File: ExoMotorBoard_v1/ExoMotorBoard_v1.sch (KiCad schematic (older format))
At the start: 3 parts, among them IC1 DSPIC33FJ128MC802-I_SP, U1 MIC5219-3.3YMM

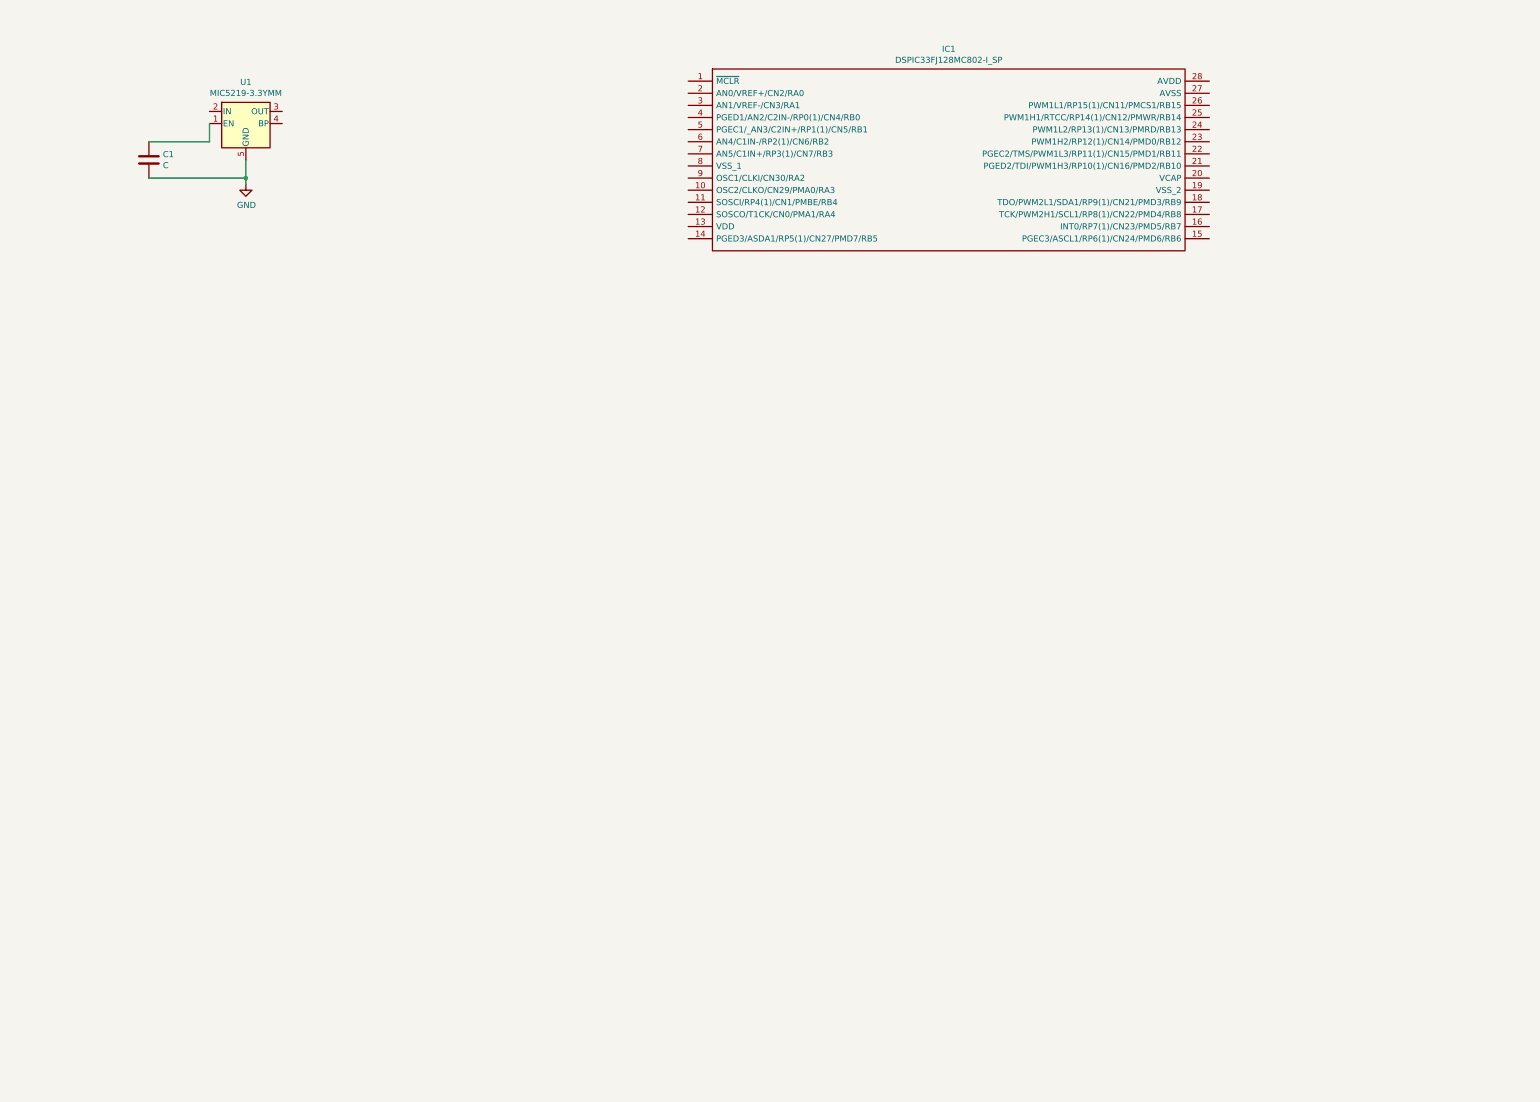
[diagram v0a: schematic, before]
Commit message: 3.3v regulator circuit updated
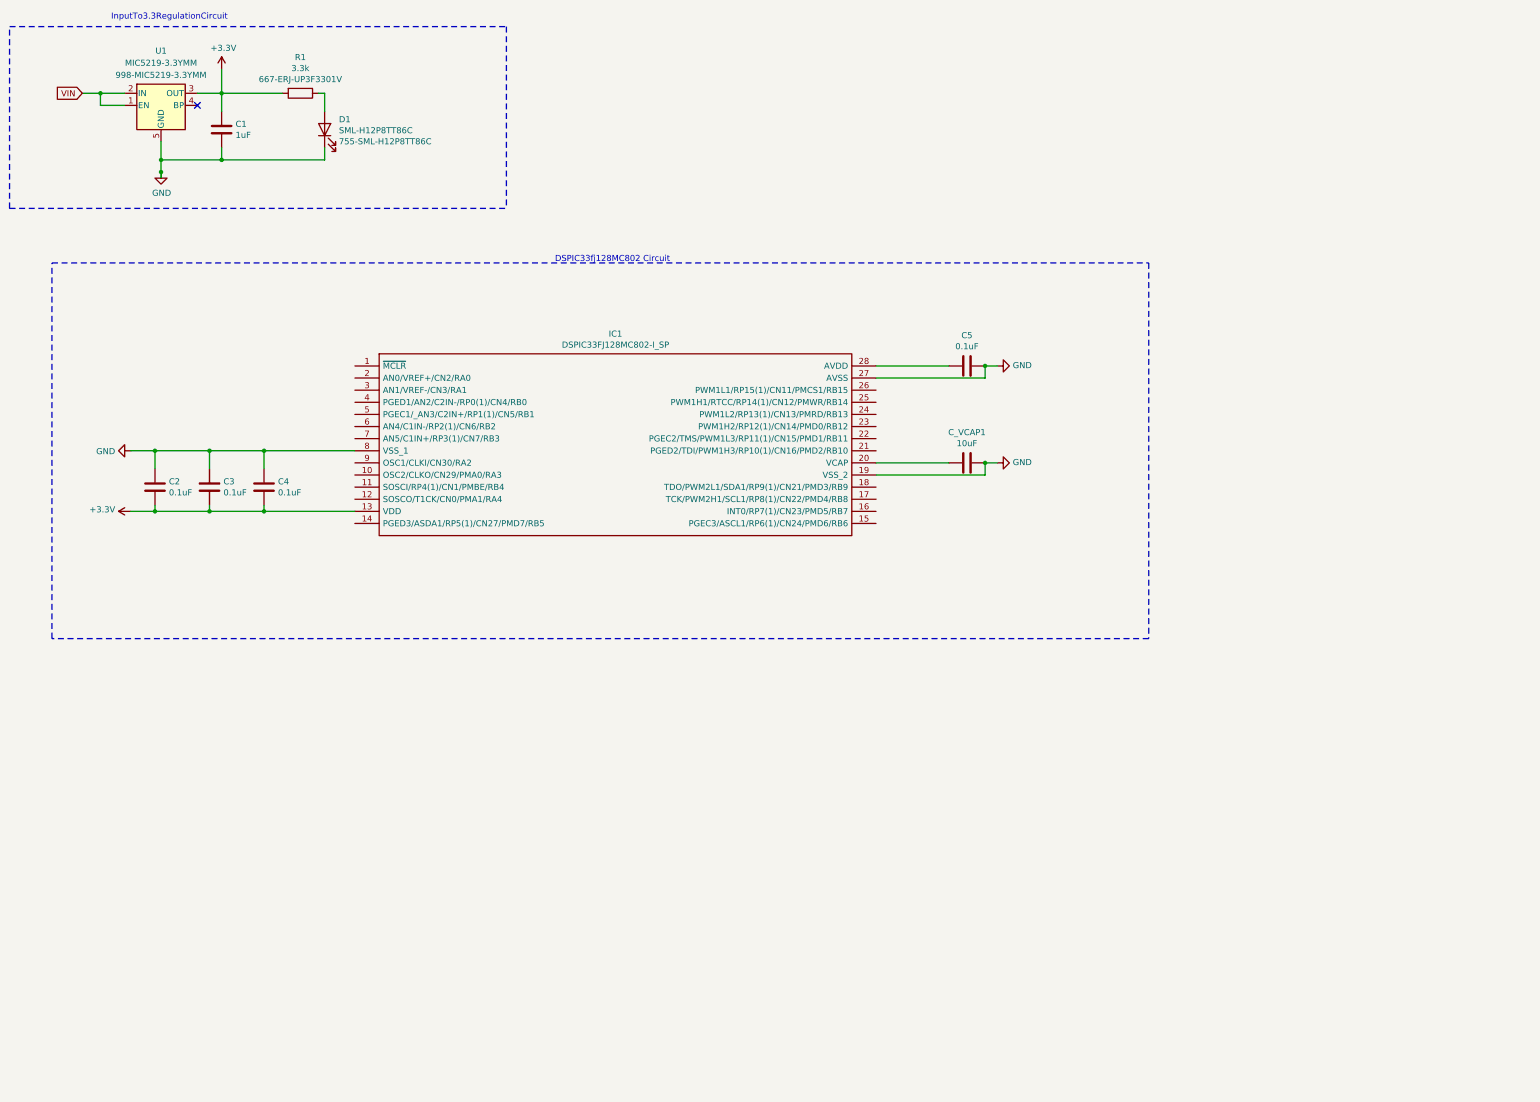
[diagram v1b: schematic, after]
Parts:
- added C2, C3, C4, C5: 0.1uF, Capacitor_SMD:C_0805_2012Metric_Pad1.18x1.45mm_HandSolder, symbol Device:C
- added C_VCAP1: 10uF, Capacitor_SMD:C_0805_2012Metric_Pad1.18x1.45mm_HandSolder, symbol Device:C
- added D1: SML-H12P8TT86C, LED_SMD:LED_0805_2012Metric_Pad1.15x1.40mm_HandSolder, symbol Device:LED
- added R1: 3.3k, Resistor_SMD:R_0603_1608Metric_Pad0.98x0.95mm_HandSolder, symbol Device:R
- C1: value C -> 1uF; footprint Capacitor_SMD:CP_Elec_4x5.3 -> Capacitor_SMD:C_0805_2012Metric_Pad1.18x1.45mm_HandSolder
- U1: Mouser (none) -> 998-MIC5219-3.3YMM
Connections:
- net labels added: +3.3V, VIN
- wire segments 5 -> 39
- no-connect marks 0 -> 1
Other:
- note added: "DSPIC33fj128MC802 Circuit"
- note added: "InputTo3.3RegulationCircuit\n"
- moved on the sheet: C1, IC1, U1

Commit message: Kicad project organized by modular sheets
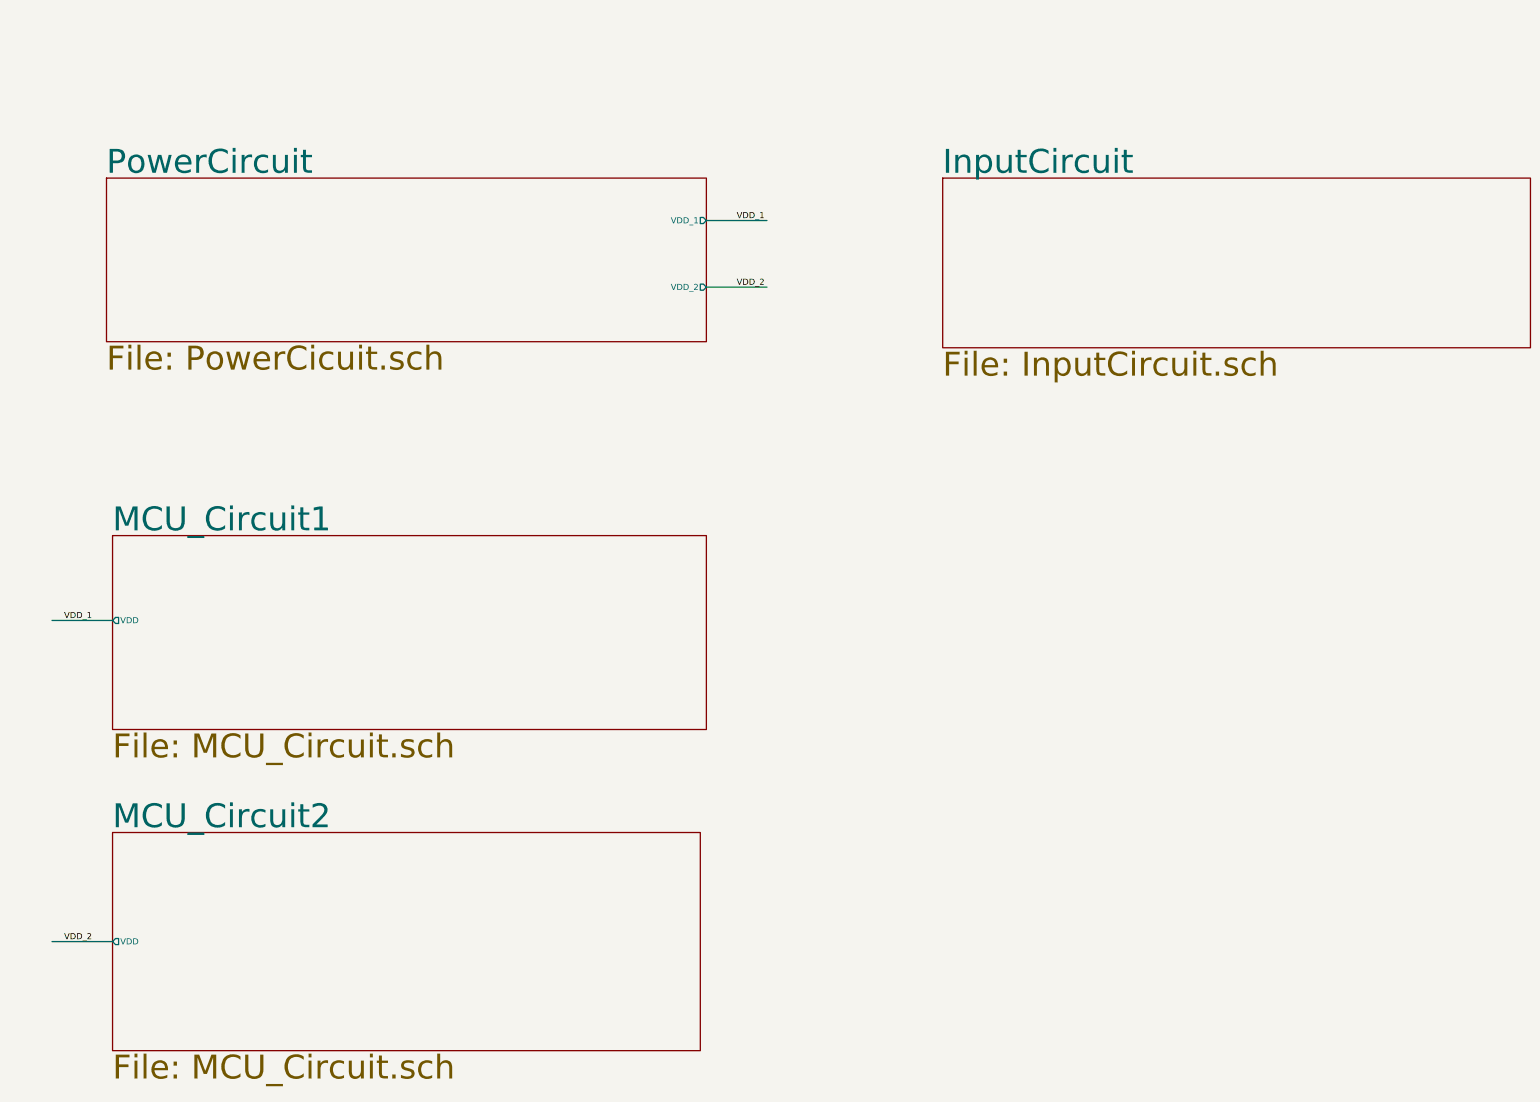
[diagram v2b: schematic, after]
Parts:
- removed C1: 1uF, Capacitor_SMD:C_0805_2012Metric_Pad1.18x1.45mm_HandSolder, symbol Device:C
- removed C2, C3, C4, C5: 0.1uF, Capacitor_SMD:C_0805_2012Metric_Pad1.18x1.45mm_HandSolder, symbol Device:C
- removed C_VCAP1: 10uF, Capacitor_SMD:C_0805_2012Metric_Pad1.18x1.45mm_HandSolder, symbol Device:C
- removed D1: SML-H12P8TT86C, LED_SMD:LED_0805_2012Metric_Pad1.15x1.40mm_HandSolder, symbol Device:LED
- removed IC1: DSPIC33FJ128MC802-I_SP, DSPIC33FJ128MC802-I_SP:DIP794W56P254L3486H508Q28N, symbol DSPIC33FJ128MC802-I_SP:DSPIC33FJ128MC802-I_SP
- removed R1: 3.3k, Resistor_SMD:R_0603_1608Metric_Pad0.98x0.95mm_HandSolder, symbol Device:R
- removed U1: MIC5219-3.3YMM, Package_SO:MSOP-8_3x3mm_P0.65mm, symbol Regulator_Linear:MIC5219-3.3YMM
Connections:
- net labels added: VDD_1, VDD_2
- net labels removed: +3.3V, GND, VIN
- wire segments 39 -> 4
- no-connect marks 1 -> 0
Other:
- note removed: "DSPIC33fj128MC802 Circuit"
- note removed: "InputTo3.3RegulationCircuit\n"

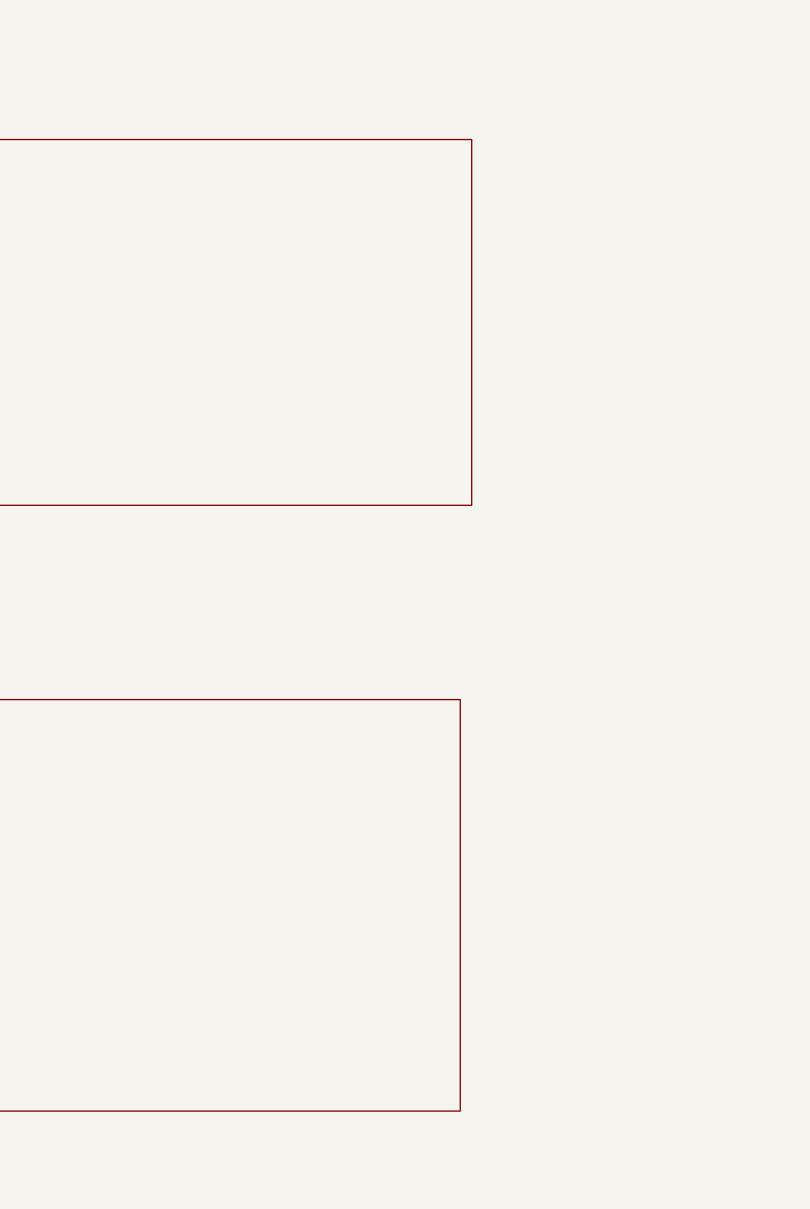
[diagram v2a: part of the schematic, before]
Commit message: MCU schematic connections updated
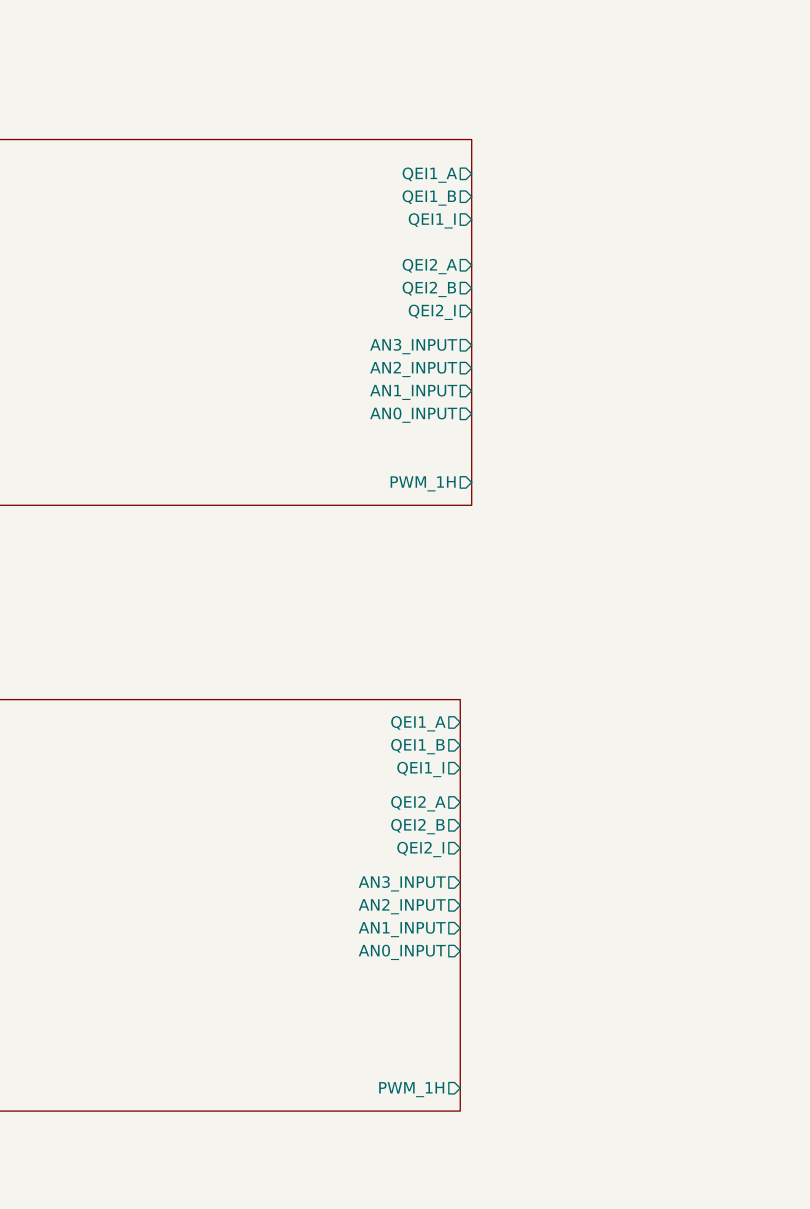
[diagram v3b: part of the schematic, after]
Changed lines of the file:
@@
 $EndDescr
-$Sheet
-S 1450 4950 4900 1600
-U 610E570F
-F0 "MCU_Circuit1" 197
-F1 "MCU_Circuit.sch" 197
-F2 "VDD" O L 1450 5650 50
-$EndSheet
 $Sheet
 S 8300 2000 4850 1400
@@
 F2 "VDD_1" O R 6350 2350 50
 F3 "VDD_2" O R 6350 2900 50
-$EndSheet
-$Sheet
-S 1450 7400 4850 1800
-U 6118F320
-F0 "MCU_Circuit2" 197
-F1 "MCU_Circuit.sch" 197
-F2 "VDD" O L 1450 8300 50
 $EndSheet
 Wire Wire Line
@@
 Text Label 1050 8300 0    50   ~ 0
 VDD_2
+$Sheet
+S 1450 4950 4900 1600
+U 610E570F
+F0 "MCU_Circuit1" 197
+F1 "MCU_Circuit.sch" 197
+F2 "VDD" O L 1450 5650 50
+F3 "QEI1_I" O R 6350 5300 50
+F4 "QEI1_B" O R 6350 5200 50
+F5 "QEI1_A" O R 6350 5100 50
+F6 "QEI2_B" O R 6350 5600 50
+F7 "QEI2_A" O R 6350 5500 50
+F8 "PWM_1H" O R 6350 6450 50
+F9 "QEI2_I" O R 6350 5700 50
+F10 "AN3_INPUT" O R 6350 5850 50
+F11 "AN2_INPUT" O R 6350 5950 50
+F12 "AN1_INPUT" O R 6350 6050 50
+F13 "AN0_INPUT" O R 6350 6150 50
+$EndSheet
+$Sheet
+S 1450 7400 4850 1800
+U 6118F320
+F0 "MCU_Circuit2" 197
+F1 "MCU_Circuit.sch" 197
+F2 "VDD" O L 1450 8300 50
+F3 "QEI1_I" O R 6300 7700 50
+F4 "QEI1_B" O R 6300 7600 50
+F5 "QEI1_A" O R 6300 7500 50
+F6 "QEI2_B" O R 6300 7950 50
+F7 "QEI2_A" O R 6300 7850 50
+F8 "PWM_1H" O R 6300 9100 50
+F9 "QEI2_I" O R 6300 8050 50
+F10 "AN3_INPUT" O R 6300 8200 50
+F11 "AN2_INPUT" O R 6300 8300 50
+F12 "AN1_INPUT" O R 6300 8400 50
+F13 "AN0_INPUT" O R 6300 8500 50
+$EndSheet
 $EndSCHEMATC
